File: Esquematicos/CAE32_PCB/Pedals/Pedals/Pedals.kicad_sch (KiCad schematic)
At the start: 19 parts, among them J1 SPI_MASTER, J2 CAN, J3 PGRM and SPI, SW1 CONFIG, SW2 BOOT, SW3 RST, U1 STM32F072RBTx

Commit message: chore: arrange schematics components
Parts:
- C1: footprint Capacitor_SMD:C_0603_1608Metric_Pad1.08x0.95mm_HandSolder -> Capacitor_SMD:C_0603_1608Metric
- D1, D2, D3: footprint LED_SMD:LED_0805_2012Metric_Pad1.15x1.40mm_HandSolder -> LED_SMD:LED_0805_2012Metric
- R1, R2, R3, R4: footprint Resistor_SMD:R_0603_1608Metric_Pad0.98x0.95mm_HandSolder -> Resistor_SMD:R_0603_1608Metric

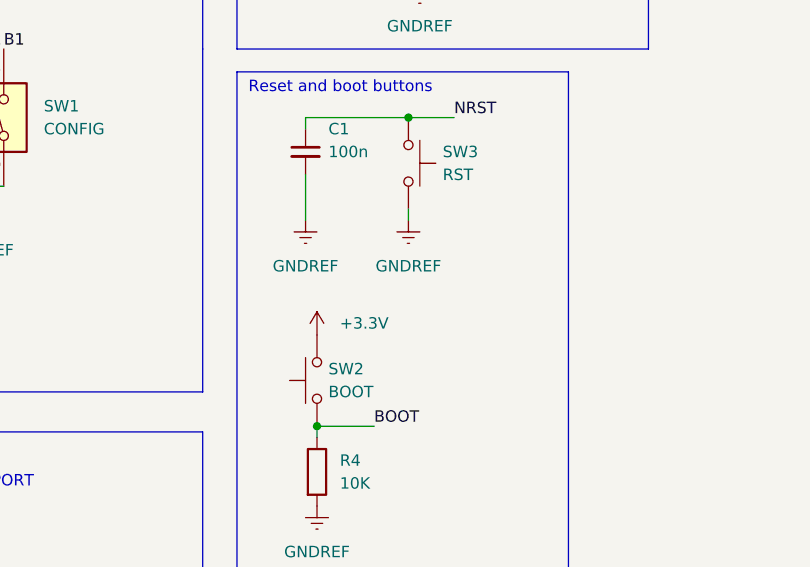
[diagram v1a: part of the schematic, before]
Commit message: update: added minor improvements to Pedal's PCB
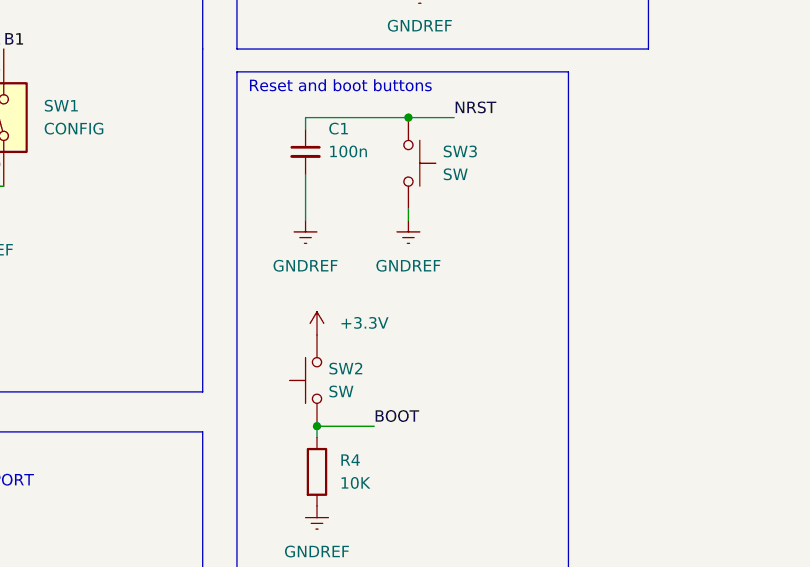
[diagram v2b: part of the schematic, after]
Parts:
- SW2: value BOOT -> SW
- SW3: value RST -> SW
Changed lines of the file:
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@@
       (effects (font (size 1.27 1.27)) (justify left))
     )
-    (property "Value" "RST" (at 257.81 77.4699 90)
+    (property "Value" "SW" (at 257.81 77.4699 90)
       (effects (font (size 1.27 1.27)) (justify left))
     )
@@
       (effects (font (size 1.27 1.27)) (justify right))
     )
-    (property "Value" "BOOT" (at 245.11 101.5999 90)
-      (effects (font (size 1.27 1.27)) (justify right))
-    )
+    (property "Value" "SW" (at 245.11 101.5999 90)
+      (effects (font (size 1.27 1.27)) (justify right))
+    )

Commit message: update: PCB pedals Version:2.1.1
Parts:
- removed J1: SPI_MASTER, Connector_PinSocket_2.54mm:PinSocket_1x05_P2.54mm_Vertical, symbol Connector:Conn_01x05_Female
- removed J2: CAN, Connector_PinHeader_2.54mm:PinHeader_1x02_P2.54mm_Vertical, symbol Connector:Conn_01x02_Male
- removed J3: PGRM and SPI, Connector_RJ:RJ45_Amphenol_RJHSE538X, symbol Connector:8P8C_LED_Shielded
- added J1: Conn_01x19_Pin, Connector_FFC-FPC:TE_1-84953-7_1x17-1MP_P1.0mm_Horizontal, symbol Connector:Conn_01x19_Pin
- H1, H2, H3, H4: footprint MountingHole:MountingHole_2.2mm_M2_DIN965_Pad -> MountingHole:MountingHole_3.2mm_M3_DIN965_Pad_TopBottom
- SW2, SW3: footprint Extra_components:TS-1095PD-A16B2-D2 -> Button_Switch_SMD:SW_SPST_TL3342; Item C2834890 -> C2886897; LCSC_PART C2834890 -> C2886897; Vendor C2834890 -> C2886897
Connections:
- net +3.3V: now also J1.2 (Pin_2)
- net +5V: now also J1.1 (Pin_1)
- net BOOT: now also J1.7 (Pin_7)
- net CAN_RX: now also J1.14 (Pin_14)
- net CAN_TX: now also J1.15 (Pin_15)
- net CS_ADC: now also J1.10 (Pin_10)
- net DIN: now also J1.13 (Pin_13)
- net DOUT: now also J1.12 (Pin_12)
- net GNDREF: now also J1.16 (Pin_16), J1.17 (Pin_17), J1.MP
- net PGR_UART_RX: now also J1.9 (Pin_9)
- net PGR_UART_TX: now also J1.8 (Pin_8)
- net SCKL: now also J1.11 (Pin_11)
- net S_CKL: now also J1.3 (Pin_3)
- net S_CS_PEDALS: now also J1.4 (Pin_4)
- net S_DIN: now also J1.5 (Pin_5)
- net S_DOUT: now also J1.6 (Pin_6)
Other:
- note added: "(UART) Programming an Debugging port"
- note added: "CAN"
- note added: "SPI_Expansion"
- note added: "SPI_Master"
- note removed: "Data connector"
- note removed: "SPI Master and CAN PORT"
- moved on the sheet: C1, D1, D2, D3, H1, H2, H3, H4, R1, R2, R3, R4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
